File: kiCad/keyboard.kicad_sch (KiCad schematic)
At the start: 123 parts, among them J0 Conn_01x03, SW1 MX, SW10 MX, SW11 MX, SW12 MX, SW13 MX, SW14 MX, SW15 MX, SW16 MX, SW17 MX, SW18 MX, SW19 MX, SW2 MX, SW20 MX, SW21 MX, SW22 MX, SW23 MX, SW24 MX, SW25 MX, SW26 MX, SW27 MX, SW28 MX, SW29 MX, SW3 MX, SW30 MX, SW31 MX, SW32 MX, SW33 MX, SW34 MX, SW35 MX, SW36 MX, SW37 MX, SW38 MX, SW39 MX, SW4 MX, SW40 MX, SW41 MX, SW42 MX, SW43 MX, SW44 MX, SW45 MX, SW46 MX, SW47 MX, SW48 MX, SW49 MX, SW5 MX, SW50 MX, SW51 MX, SW52 MX, SW53 MX, SW54 MX, SW55 MX, SW56 MX, SW57 MX, SW58 MX, SW59 MX, SW6 MX, SW60 MX, SW61 MX, SW7 MX, SW8 MX, SW9 MX, U0 Sparkfun_Pro_Micro

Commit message: add library submodules
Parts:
- U0: footprint Arduino:Sparkfun_Pro_Micro -> Keebio-Parts:ArduinoProMicro
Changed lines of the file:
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@@
       (effects (font (size 1.524 1.524)))
     )
-    (property "Footprint" "Arduino:Sparkfun_Pro_Micro" (id 2) (at 41.91 64.77 0)
+    (property "Footprint" "Keebio-Parts:ArduinoProMicro" (id 2) (at 41.91 64.77 0)
       (effects (font (size 1.524 1.524)) hide)
     )
@@
     )
     (path "/7fc6bb76-8a4f-42da-9619-6ff8c2a859d3"
-      (reference "U0") (unit 1) (value "Sparkfun_Pro_Micro") (footprint "Arduino:Sparkfun_Pro_Micro")
-    )
-  )
+      (reference "U0") (unit 1) (value "Sparkfun_Pro_Micro") (footprint "Keebio-Parts:ArduinoProMicro")
+    )
+  )

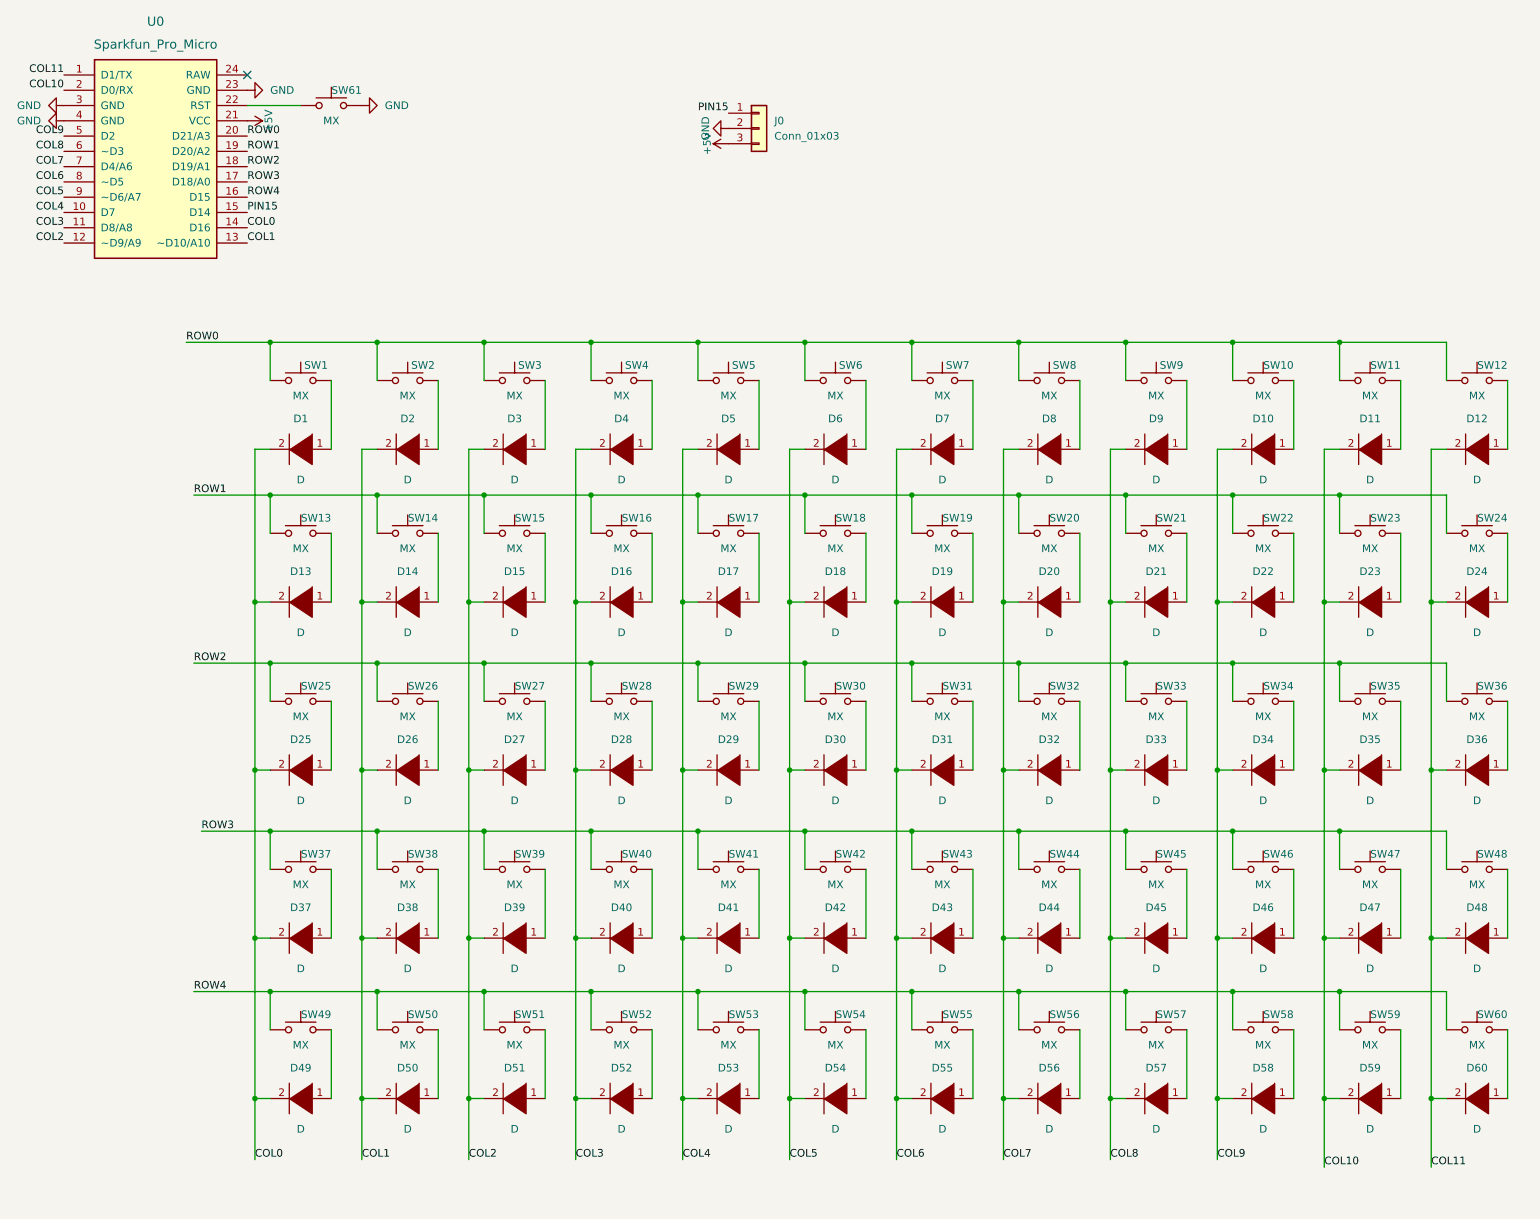
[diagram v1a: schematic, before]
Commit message: draw pcb, add more footprints
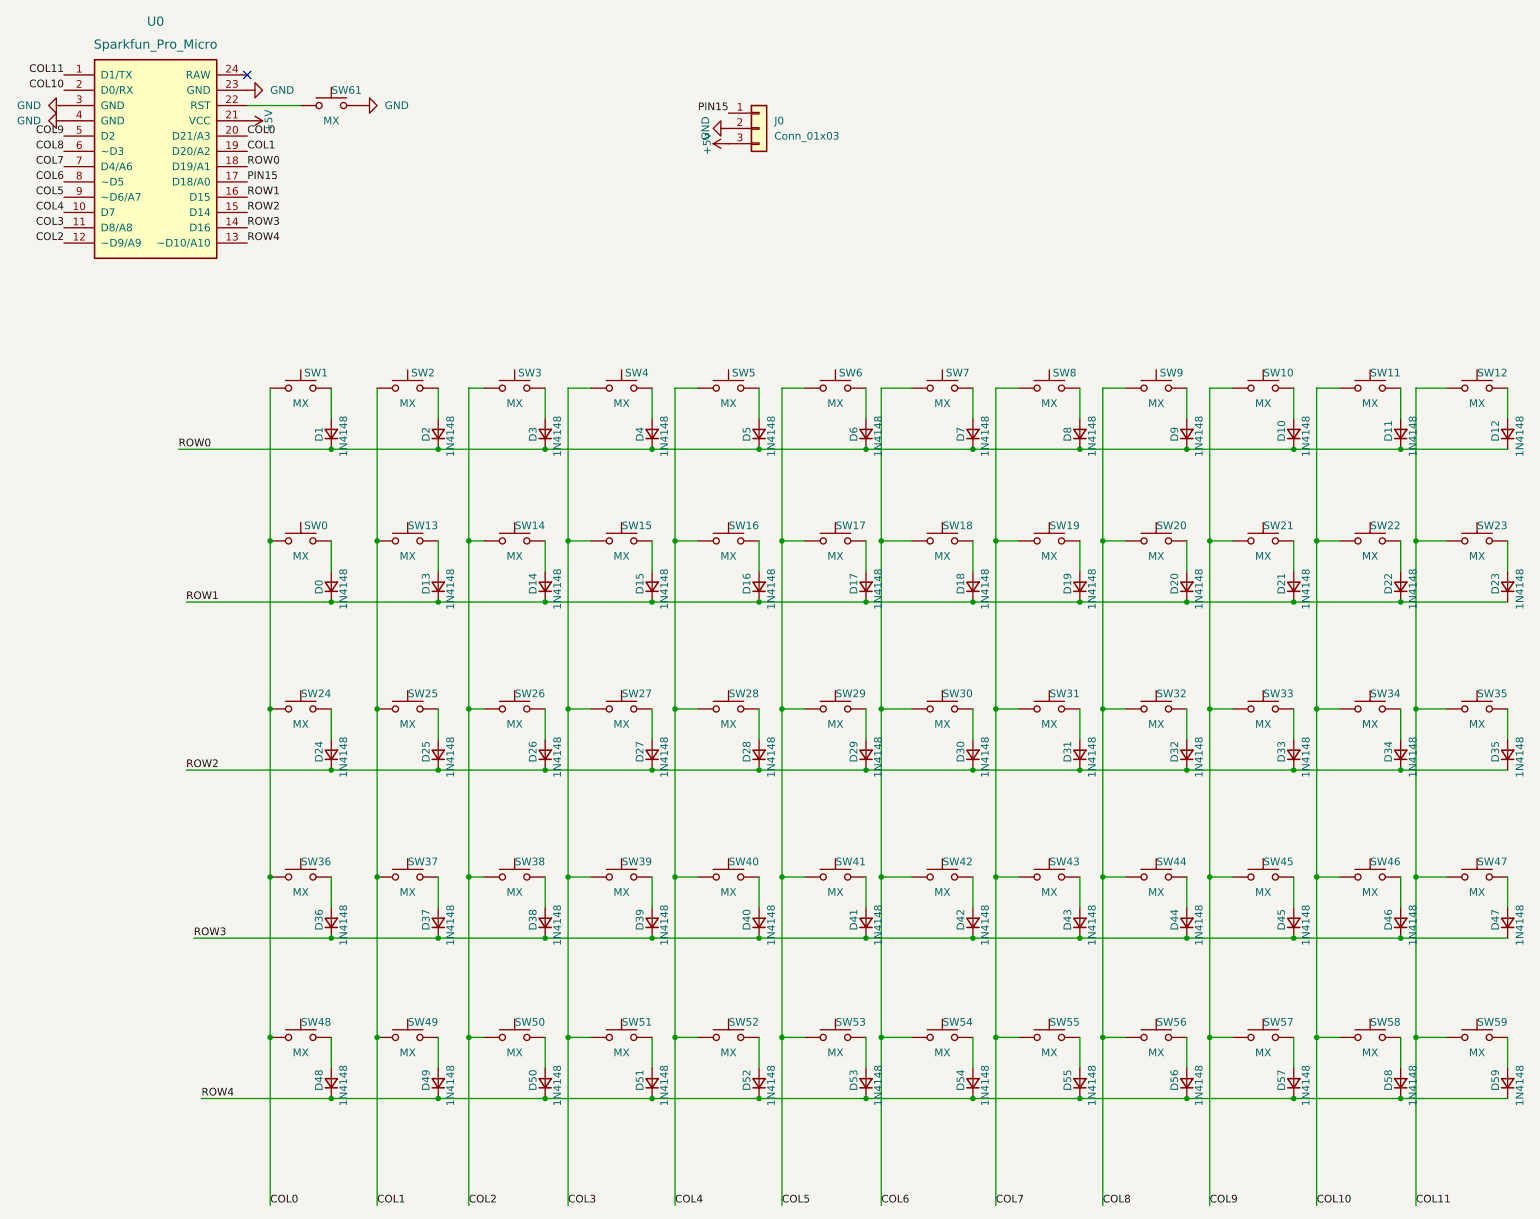
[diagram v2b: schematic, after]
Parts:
- removed D1, D10, D11, D12, D13, D14, D15, D16, D17, D18, D19, D2, D20, D21, D22, D23, D24, D25, D26, D27, D28, D29, D3, D30, D31, D32, D33, D34, D35, D36, D37, D38, D39, D4, D40, D41, D42, D43, D44, D45, D46, D47, D48, D49, D5, D50, D51, D52, D53, D54, D55, D56, D57, D58, D59, D6, D60, D7, D8, D9: D, Diode_THT:D_DO-35_SOD27_P7.62mm_Horizontal, symbol pspice:DIODE
- removed SW60: MX, Button_Switch_Keyboard:SW_Cherry_MX_1.00u_PCB, symbol Switch:SW_Push
- added D0, D1, D10, D11, D12, D13, D14, D15, D16, D17, D18, D19, D2, D20, D21, D22, D23, D24, D25, D26, D27, D28, D29, D3, D30, D31, D32, D33, D34, D35, D36, D37, D38, D39, D4, D40, D41, D42, D43, D44, D45, D46, D47, D48, D49, D5, D50, D51, D52, D53, D54, D55, D56, D57, D58, D59, D6, D7, D8, D9: 1N4148, Diode_THT:D_DO-35_SOD27_P7.62mm_Horizontal, symbol Device:D_Small
- added SW0: MX, MX_Alps_Hybrid:MX-1U-NoLED, symbol Switch:SW_Push
- SW1, SW10, SW11, SW12, SW13, SW14, SW15, SW16, SW17, SW18, SW19, SW2, SW20, SW21, SW22, SW23, SW24, SW25, SW26, SW27, SW28, SW29, SW3, SW30, SW31, SW32, SW33, SW34, SW35, SW36, SW37, SW38, SW39, SW4, SW40, SW41, SW42, SW43, SW44, SW45, SW46, SW47, SW48, SW49, SW5, SW50, SW51, SW52, SW53, SW54, SW55, SW56, SW57, SW58, SW59, SW6, SW7, SW8, SW9: footprint Button_Switch_Keyboard:SW_Cherry_MX_1.00u_PCB -> MX_Alps_Hybrid:MX-1U-NoLED
- SW61: footprint Button_Switch_Keyboard:SW_Cherry_MX_1.00u_PCB -> Molex-0548190589:PushButton_6x6mm_TH_Pretty
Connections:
- net COL0: now also SW1.1, SW24.1, SW36.1, SW48.1, U0.20 (D21/A3), SW0.1; no longer U0.14 (D16)
- net COL1: now also SW13.1, SW2.1, SW25.1, SW37.1, SW49.1, U0.19 (D20/A2); no longer U0.13 (~D10/A10)
- net COL10: now also SW11.1, SW22.1, SW34.1, SW46.1, SW58.1
- net COL11: now also SW12.1, SW23.1, SW35.1, SW47.1, SW59.1
- net COL2: now also SW14.1, SW26.1, SW3.1, SW38.1, SW50.1
- net COL3: now also SW15.1, SW27.1, SW39.1, SW4.1, SW51.1
- net COL4: now also SW16.1, SW28.1, SW40.1, SW5.1, SW52.1
- net COL5: now also SW17.1, SW29.1, SW41.1, SW53.1, SW6.1
- net COL6: now also SW18.1, SW30.1, SW42.1, SW54.1, SW7.1
- net COL7: now also SW19.1, SW31.1, SW43.1, SW55.1, SW8.1
- net COL8: now also SW20.1, SW32.1, SW44.1, SW56.1, SW9.1
- net COL9: now also SW10.1, SW21.1, SW33.1, SW45.1, SW57.1
- net PIN15: now also U0.17 (D18/A0); no longer U0.15 (D14)
- net ROW0: now also U0.18 (D19/A1), D1.1 (K), D10.1 (K), D11.1 (K), D12.1 (K), D2.1 (K), D3.1 (K), D4.1 (K), D5.1 (K), D6.1 (K), D7.1 (K), D8.1 (K), D9.1 (K); no longer SW1.1, SW10.1, SW11.1, SW12.1, SW2.1, SW3.1, SW4.1, SW5.1, SW6.1, SW7.1, SW8.1, SW9.1, U0.20 (D21/A3)
- net ROW1: now also U0.16 (D15), D0.1 (K), D13.1 (K), D14.1 (K), D15.1 (K), D16.1 (K), D17.1 (K), D18.1 (K), D19.1 (K), D20.1 (K), D21.1 (K), D22.1 (K), D23.1 (K); no longer SW13.1, SW14.1, SW15.1, SW16.1, SW17.1, SW18.1, SW19.1, SW20.1, SW21.1, SW22.1, SW23.1, SW24.1, U0.19 (D20/A2)
- net ROW2: now also U0.15 (D14), D24.1 (K), D25.1 (K), D26.1 (K), D27.1 (K), D28.1 (K), D29.1 (K), D30.1 (K), D31.1 (K), D32.1 (K), D33.1 (K), D34.1 (K), D35.1 (K); no longer SW25.1, SW26.1, SW27.1, SW28.1, SW29.1, SW30.1, SW31.1, SW32.1, SW33.1, SW34.1, SW35.1, SW36.1, U0.18 (D19/A1)
- net ROW3: now also U0.14 (D16), D36.1 (K), D37.1 (K), D38.1 (K), D39.1 (K), D40.1 (K), D41.1 (K), D42.1 (K), D43.1 (K), D44.1 (K), D45.1 (K), D46.1 (K), D47.1 (K); no longer SW37.1, SW38.1, SW39.1, SW40.1, SW41.1, SW42.1, SW43.1, SW44.1, SW45.1, SW46.1, SW47.1, SW48.1, U0.17 (D18/A0)
- net ROW4: now also U0.13 (~D10/A10), D48.1 (K), D49.1 (K), D50.1 (K), D51.1 (K), D52.1 (K), D53.1 (K), D54.1 (K), D55.1 (K), D56.1 (K), D57.1 (K), D58.1 (K), D59.1 (K); no longer SW49.1, SW50.1, SW51.1, SW52.1, SW53.1, SW54.1, SW55.1, SW56.1, SW57.1, SW58.1, SW59.1, U0.16 (D15)
- net at SW21.2: now also D21.2 (A)
- net at SW3.2: now also D3.2 (A)
- net at SW19.2: now also D19.2 (A)
- net at SW6.2: now also D6.2 (A)
- net at SW53.2: now also D53.2 (A)
- net at SW22.2: now also D22.2 (A)
- net at SW23.2: now also D23.2 (A)
- net at SW42.2: now also D42.2 (A)
- net at SW13.2: now also D13.2 (A)
- net at SW58.2: now also D58.2 (A)
- net at SW54.2: now also D54.2 (A)
- net at SW48.2: now also D48.2 (A)
- net at SW29.2: now also D29.2 (A)
- net at SW39.2: now also D39.2 (A)
- net at SW45.2: now also D45.2 (A)
- net at SW2.2: now also D2.2 (A)
- net at SW52.2: now also D52.2 (A)
- net at SW59.2: now also D59.2 (A)
- net at SW41.2: now also D41.2 (A)
- net at SW8.2: now also D8.2 (A)
- net at SW20.2: now also D20.2 (A)
- net at SW50.2: now also D50.2 (A)
- net at SW44.2: now also D44.2 (A)
- net at SW14.2: now also D14.2 (A)
- net at SW30.2: now also D30.2 (A)
- net at SW16.2: now also D16.2 (A)
- net at SW51.2: now also D51.2 (A)
- net at SW47.2: now also D47.2 (A)
- net at SW55.2: now also D55.2 (A)
- net at SW40.2: now also D40.2 (A)
- net at SW49.2: now also D49.2 (A)
- net at SW32.2: now also D32.2 (A)
- net at SW34.2: now also D34.2 (A)
- net at SW12.2: now also D12.2 (A)
- net at SW35.2: now also D35.2 (A)
- net at SW28.2: now also D28.2 (A)
- net at SW5.2: now also D5.2 (A)
- net at SW43.2: now also D43.2 (A)
- net at SW57.2: now also D57.2 (A)
- net at SW26.2: now also D26.2 (A)
- net at SW25.2: now also D25.2 (A)
- net at SW10.2: now also D10.2 (A)
- net at SW15.2: now also D15.2 (A)
- net at SW9.2: now also D9.2 (A)
- net at SW38.2: now also D38.2 (A)
- net at SW31.2: now also D31.2 (A)
- net at SW11.2: now also D11.2 (A)
- net at SW27.2: now also D27.2 (A)
- net at SW7.2: now also D7.2 (A)
- net at SW4.2: now also D4.2 (A)
- net at SW37.2: now also D37.2 (A)
- net at SW36.2: now also D36.2 (A)
- net at SW18.2: now also D18.2 (A)
- net at SW1.2: now also D1.2 (A)
- net at SW17.2: now also D17.2 (A)
- net at SW56.2: now also D56.2 (A)
- net at SW24.2: now also D24.2 (A)
- net at SW46.2: now also D46.2 (A)
- net at SW33.2: now also D33.2 (A)
- new net: D0.2 (A), SW0.2
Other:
- moved on the sheet: SW1, SW10, SW11, SW12, SW2, SW3, SW4, SW5, SW6, SW7, SW8, SW9
